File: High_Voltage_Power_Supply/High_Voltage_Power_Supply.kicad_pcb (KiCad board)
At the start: 2 copper layers, 98 parts, among them J1 Conn_01x02_Female, J2 Conn_01x02_Female, J3 Conn_01x02_Female, J4 Conn_01x12_Female, Q1 Q_NMOS_GDS, Q2 Q_NMOS_GDS, Q3 Q_NMOS_GDS, Q4 Q_NIGBT_GCE, U1 LT3751-TSSOP, U10 ADR3412, U11 LM2576HVT-15, U2 LT3751-TSSOP, U3 ZXGD3004E6, U4 ZXGD3004E6, U5 MC14504B, U6 MC14504B, U7 LM7805, U8 LM7805, U9 LMV331

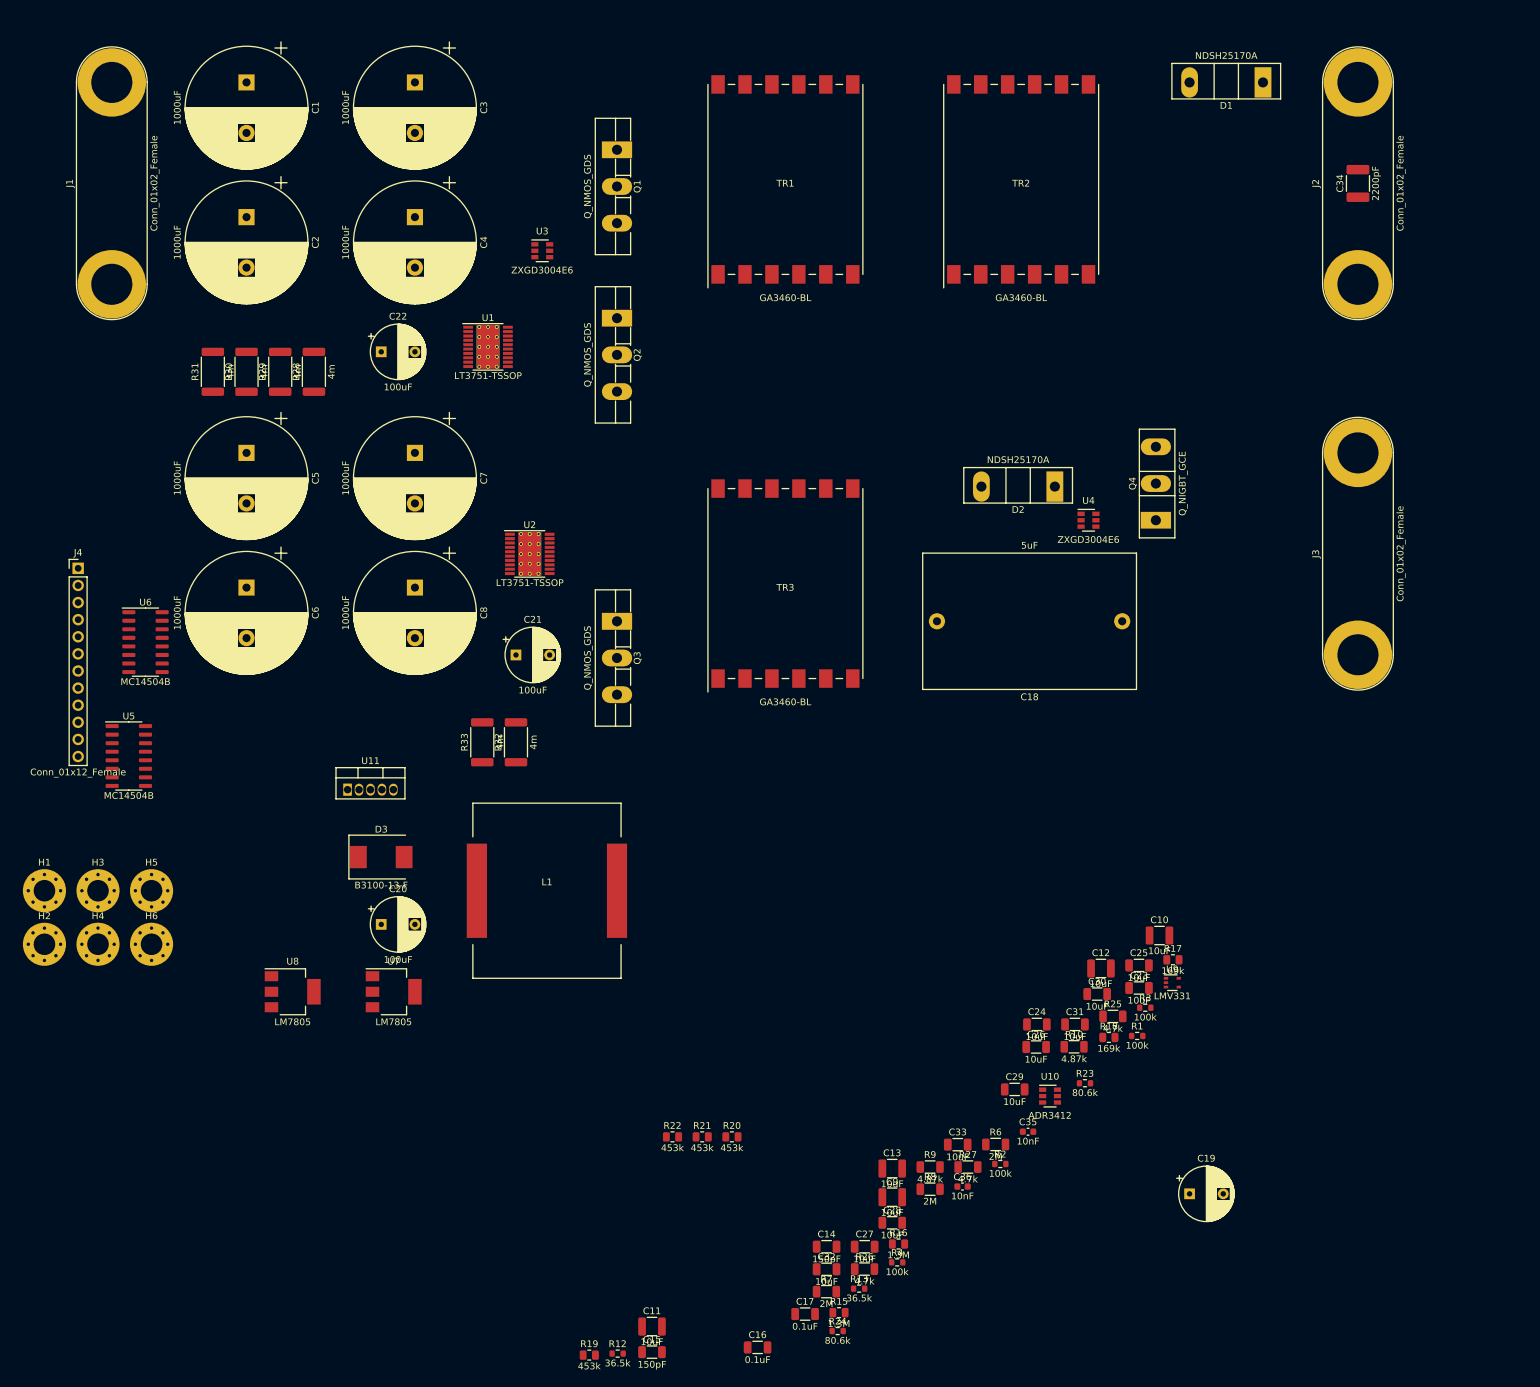
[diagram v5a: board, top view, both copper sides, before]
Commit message: Rough component placements to allow heat sinks to be installed
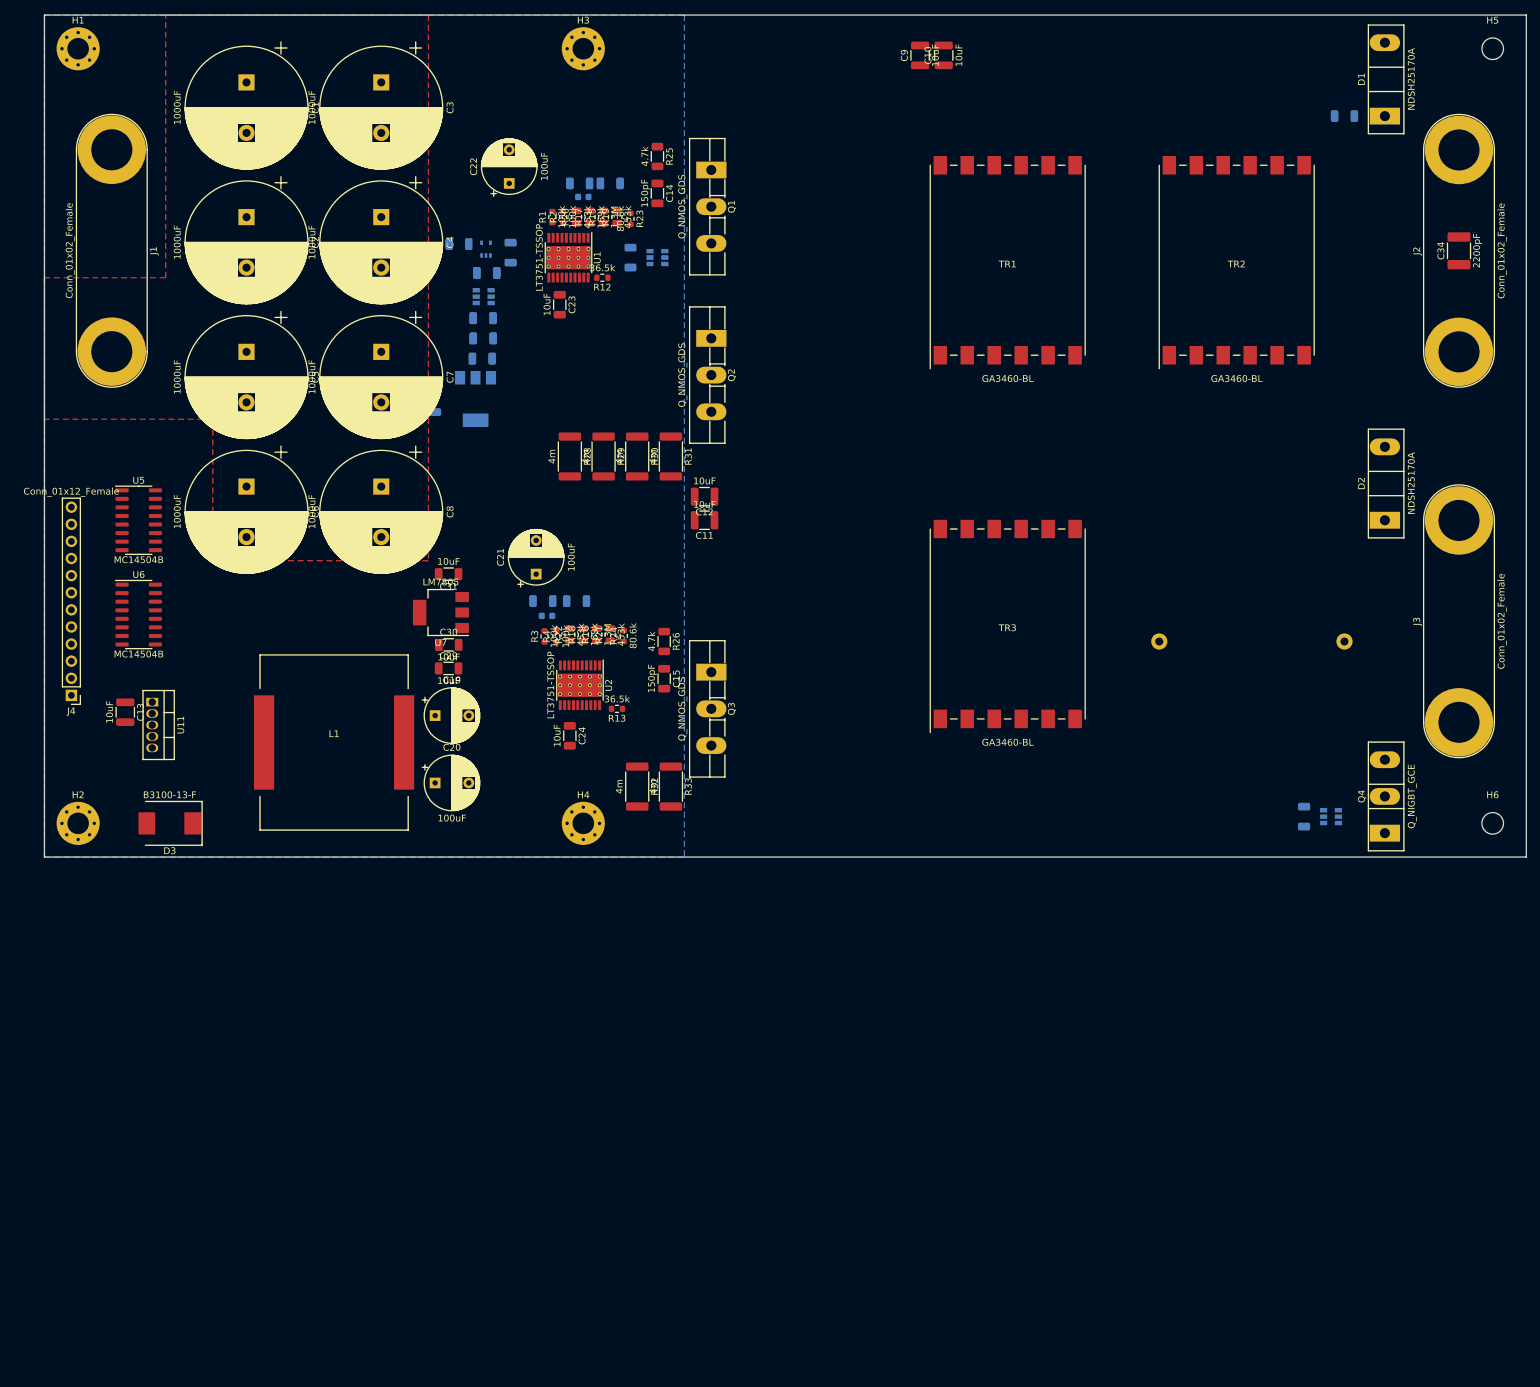
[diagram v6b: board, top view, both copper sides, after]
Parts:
- C16, C17, C18, C25, C26, C27, C28, C32, C33, C35, C36, R10, R27, R6, R7, R8, R9, U10, U3, U4, U8, U9: moved to B.Cu
- H5, H6: footprint MountingHole:MountingHole_3.2mm_M3_Pad_Via -> MountingHole:MountingHole_3.2mm_M3
- moved H5 235.1 mm to (235.0, 45.0)
- moved H6 199.9 mm to (235.0, 160.0)
- moved C9 169.6 mm to (150.0, 46.0), turned to 90 degrees
- moved R19 169.0 mm to (105.0, 70.0), turned to 90 degrees
- moved R7 167.6 mm to (104.0, 65.0), turned to 180 degrees
- moved R15 166.4 mm to (103.0, 70.0), turned to 90 degrees
- moved C17 161.6 mm to (85.7, 78.3)
- moved R6 161.2 mm to (213.0, 55.0), turned to 180 degrees
- moved R12 159.7 mm to (102.8, 79.0), turned to 180 degrees
- moved C14 158.4 mm to (111.0, 66.5), turned to 270 degrees
- moved C16 158.1 mm to (85.1, 85.0), turned to 180 degrees
- moved C27 156.7 mm to (89.2, 75.3), turned to 270 degrees
- moved R27 156.5 mm to (81.5, 74.0)
- moved R9 155.0 mm to (99.5, 65.0), turned to 180 degrees
- moved R2 154.8 mm to (97.0, 70.0), turned to 90 degrees
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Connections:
- C19 pad 1: Net-(C19-Pad1) -> VCC
- H5 pad 1: GND -> (no net)
- H6 pad 1: GND -> (no net)
- J4 pad 8: ~FAULT_IGN_5V~ -> ~FAULT_5V~
- J4 pad 9: ~FAULT_5V~ -> ~FAULT_IGN_5V~
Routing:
- added copper zone on B.Cu, net GND
- added copper zone on F.Cu, net Vtrans
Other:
- board outline added: 220 x 125 mm

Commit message: updated BOM
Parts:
- moved C21 22.5 mm to (92.0, 145.5), turned to 270 degrees
- moved C22 17.1 mm to (90.5, 82.0), turned to 270 degrees
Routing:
- net GND: track 0.00 -> 38.1 mm, vias 0 -> 19
- net ~FAULT_5V~: track 0.00 -> 9.66 mm
- net ~FAULT_IGN_5V~: track 0.00 -> 9.66 mm
- net CHARGE_5V: track 0.00 -> 7.54 mm
- net FIRE_5V: track 0.00 -> 7.54 mm
- net CHARGE_IGN_5V: track 0.00 -> 7.54 mm

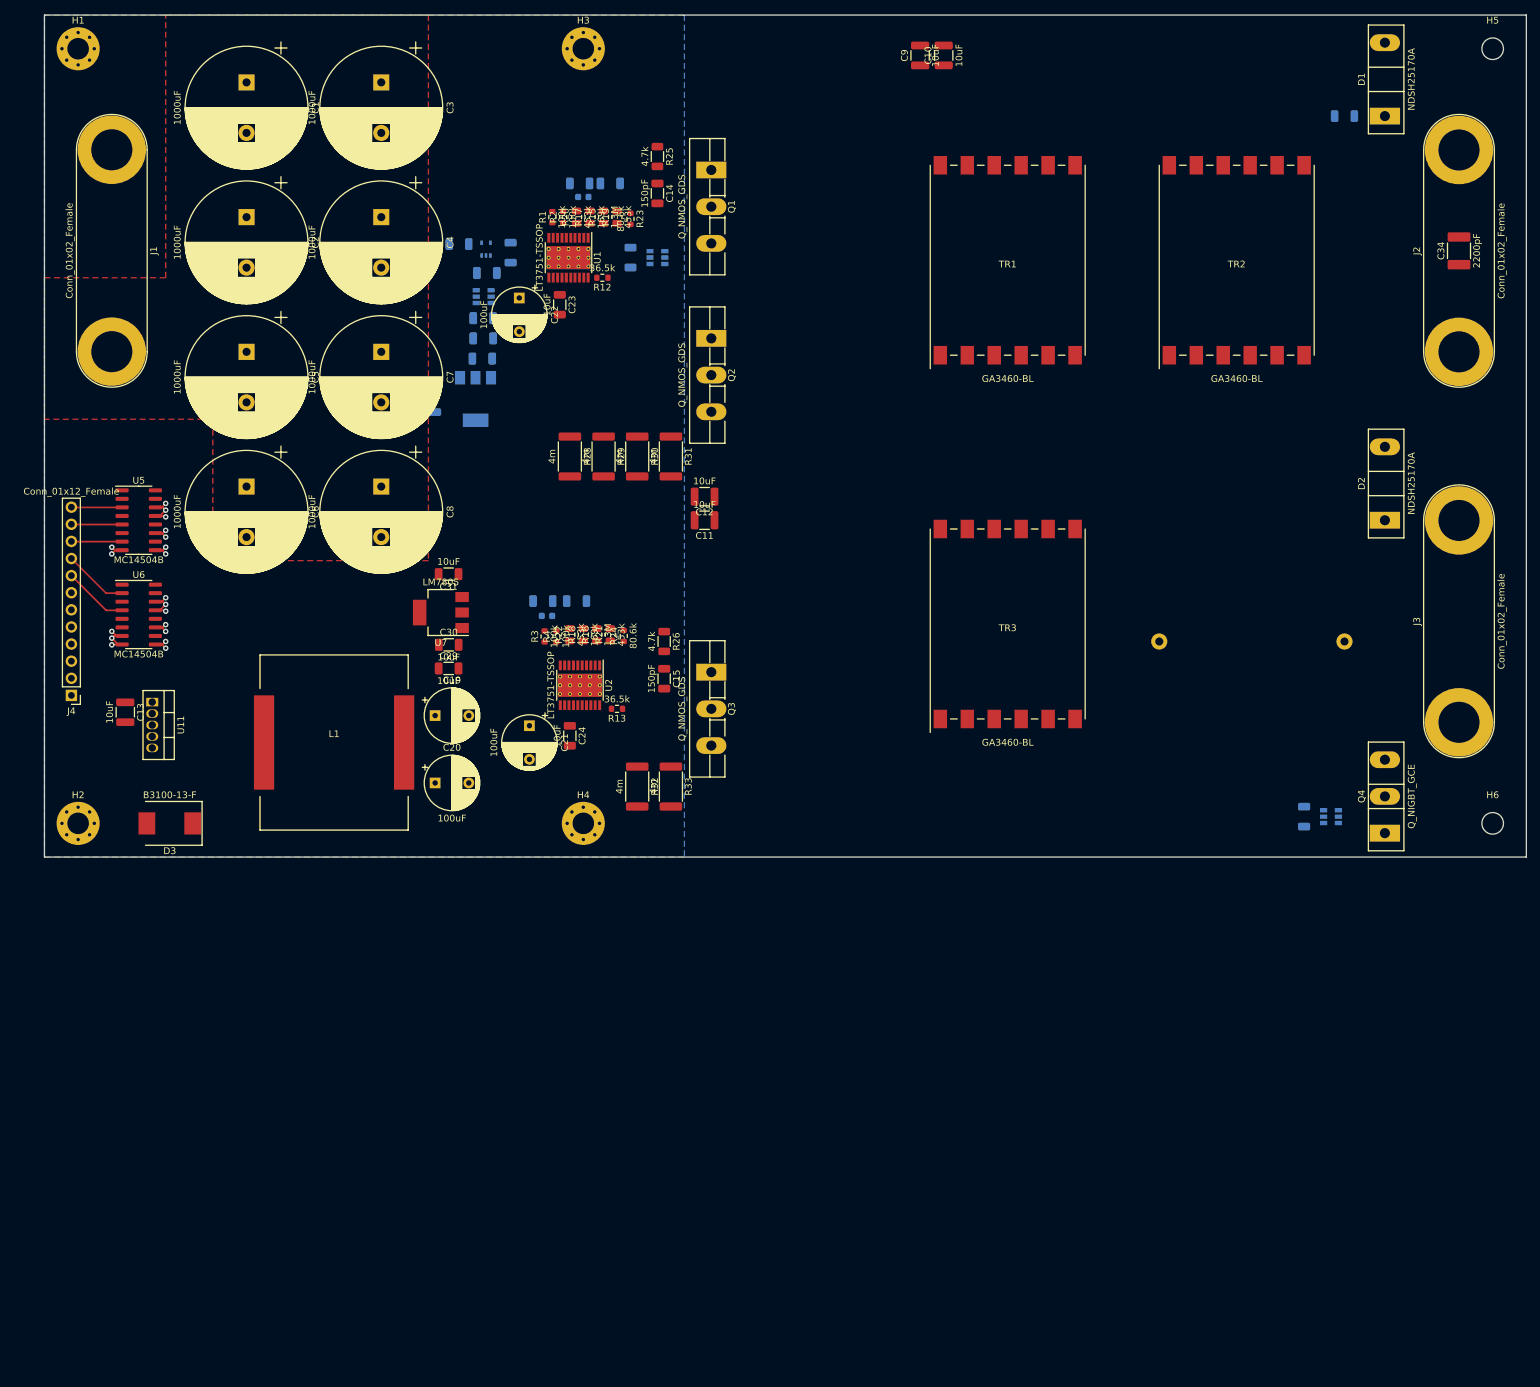
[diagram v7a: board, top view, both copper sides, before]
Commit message: routed most of the components on pcb
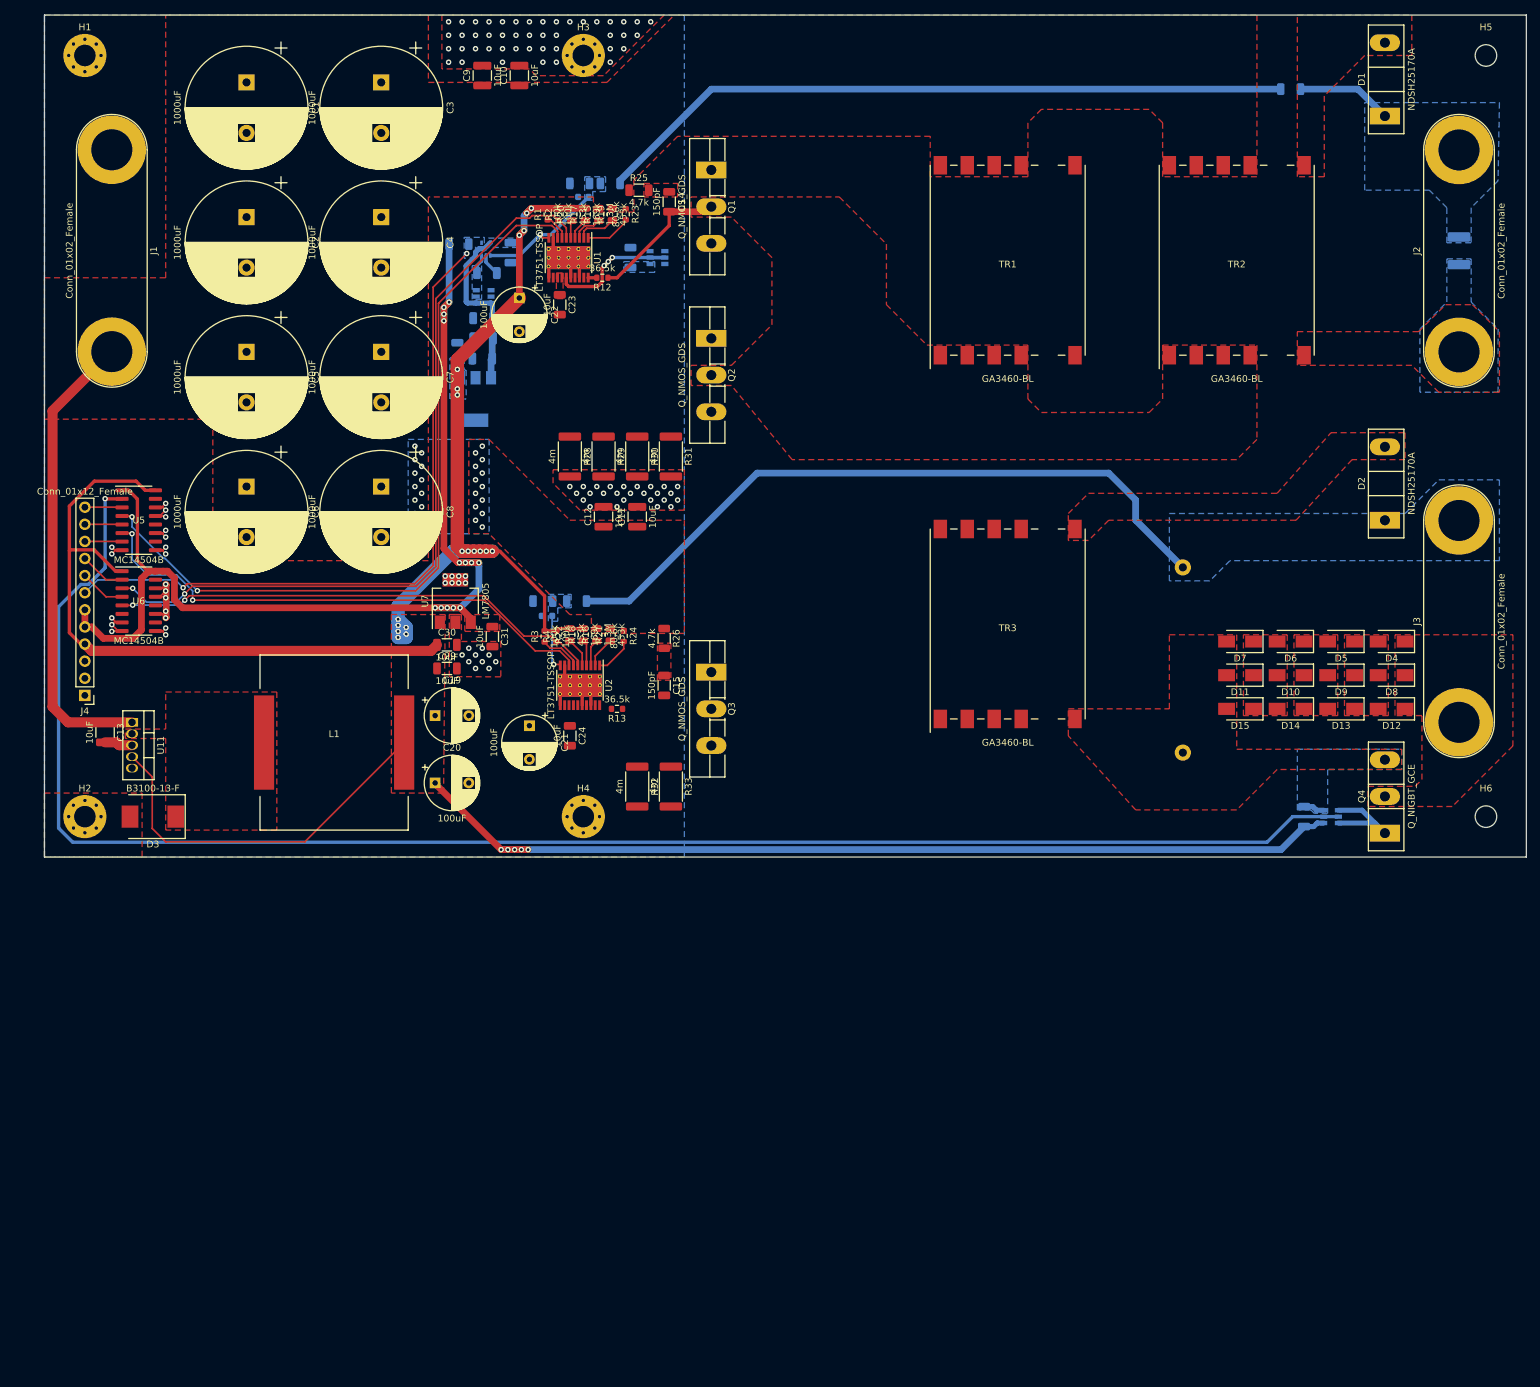
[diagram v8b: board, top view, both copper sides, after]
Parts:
- added D10: CMZ5956B, Diode_SMD:D_SMA, F.Cu at (205.0, 138.0)
- added D11: CMZ5956B, Diode_SMD:D_SMA, F.Cu at (197.5, 138.0)
- added D12: CMZ5956B, Diode_SMD:D_SMA, F.Cu at (220.0, 143.0)
- added D13: CMZ5956B, Diode_SMD:D_SMA, F.Cu at (212.5, 143.0)
- added D14: CMZ5956B, Diode_SMD:D_SMA, F.Cu at (205.0, 143.0)
- added D15: CMZ5956B, Diode_SMD:D_SMA, F.Cu at (197.5, 143.0)
- added D4: CMZ5956B, Diode_SMD:D_SMA, F.Cu at (220.0, 133.0)
- added D5: CMZ5956B, Diode_SMD:D_SMA, F.Cu at (212.5, 133.0)
- added D6: CMZ5956B, Diode_SMD:D_SMA, F.Cu at (205.0, 133.0)
- added D7: CMZ5956B, Diode_SMD:D_SMA, F.Cu at (197.5, 133.0)
- added D8: CMZ5956B, Diode_SMD:D_SMA, F.Cu at (220.0, 138.0)
- added D9: CMZ5956B, Diode_SMD:D_SMA, F.Cu at (212.5, 138.0)
- C34: moved to B.Cu
- moved C9 65.1 mm to (85.0, 49.0)
- moved C10 63.1 mm to (90.5, 49.0)
- moved C18 26.4 mm to (189.0, 122.0), turned to 270 degrees
- moved C12 15.3 mm to (103.0, 114.5), turned to 90 degrees
- moved C31 11.3 mm to (86.5, 132.3), turned to 270 degrees
- moved C11 10.0 mm to (108.0, 114.5), turned to 90 degrees
- moved R6 8.94 mm to (205.0, 51.0)
- moved C32 8.06 mm to (81.3, 90.1), turned to 90 degrees
- moved R25 5.71 mm to (108.2, 66.0), turned to 0 degrees
- moved C13 4.24 mm to (29.0, 146.5)
- moved U11 4.24 mm to (33.0, 145.0)
- moved U7 2.74 mm to (81.0, 127.0), turned to 90 degrees
- moved D3 2.69 mm to (36.1, 159.0)
- moved C14 2.15 mm to (112.8, 67.7)
- moved J4 2.00 mm to (26.0, 141.0)
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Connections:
- U5 pad 1: +5V -> +5VD
- U6 pad 16: +5V -> +5VD
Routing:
- net VCC: track 0.00 -> 415.1 mm, vias 0 -> 24
- net FIRE: track 0.00 -> 247.4 mm, vias 0 -> 1
- net +5VD: track 0.00 -> 158.9 mm, vias 0 -> 13
- net CHARGE: track 0.00 -> 116.9 mm, vias 0 -> 2
- net ~FAULT~: track 0.00 -> 116.1 mm, vias 0 -> 2
- net Net-(R6-Pad2): track 0.00 -> 104.1 mm
- net Net-(C18-Pad1): track 0.00 -> 104.0 mm
- net Charged: track 0.00 -> 102.7 mm, vias 0 -> 2
- net CHARGE_IGN: track 0.00 -> 78.0 mm, vias 0 -> 2
- net ~FAULT_IGN~: track 0.00 -> 73.0 mm, vias 0 -> 2
- net Vtrans: track 0.00 -> 69.1 mm, vias 0 -> 26
- net GND: track 38.1 -> 71.0 mm, vias 19 -> 108
- net +5VA: track 0.00 -> 25.8 mm
- net Drive_in: track 0.00 -> 22.7 mm, vias 0 -> 3
- net /Transformer/in-: track 0.00 -> 20.9 mm
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- added copper zone on B.Cu, net +5VA
- added copper zone on F.Cu, net +5VD
- added copper zone on F.Cu, net /Transformer/in-
- added copper zone on F.Cu, net /Transformer/out+
- added copper zone on B.Cu, net Charged
- added copper zone on F.Cu, net GND
- added copper zone on F.Cu, net Net-(C14-Pad1)
- added copper zone on F.Cu, net Net-(C15-Pad1)
- added copper zone on B.Cu, net Net-(C17-Pad1)
- added copper zone on B.Cu, net Net-(C18-Pad1)
- added copper zone on B.Cu, net Net-(C34-Pad1)
- added copper zone on B.Cu, net Net-(C35-Pad1)
- added copper zone on B.Cu, net Net-(C36-Pad1)
- added copper zone on F.Cu, net Net-(D10-Pad1)
- added copper zone on F.Cu, net Net-(D10-Pad2)
- added copper zone on F.Cu, net Net-(D12-Pad1)
- added copper zone on F.Cu, net Net-(D12-Pad2)
- added copper zone on F.Cu, net Net-(D2-Pad2)
- added copper zone on F.Cu, net Net-(D3-Pad1)
- added copper zone on B.Cu, net VCC
- added copper zone on F.Cu, net VCC
- added copper zone on B.Cu, net Vtrans
